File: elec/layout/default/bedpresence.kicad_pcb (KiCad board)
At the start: 2 copper layers, 40 x 40 mm, 0 parts

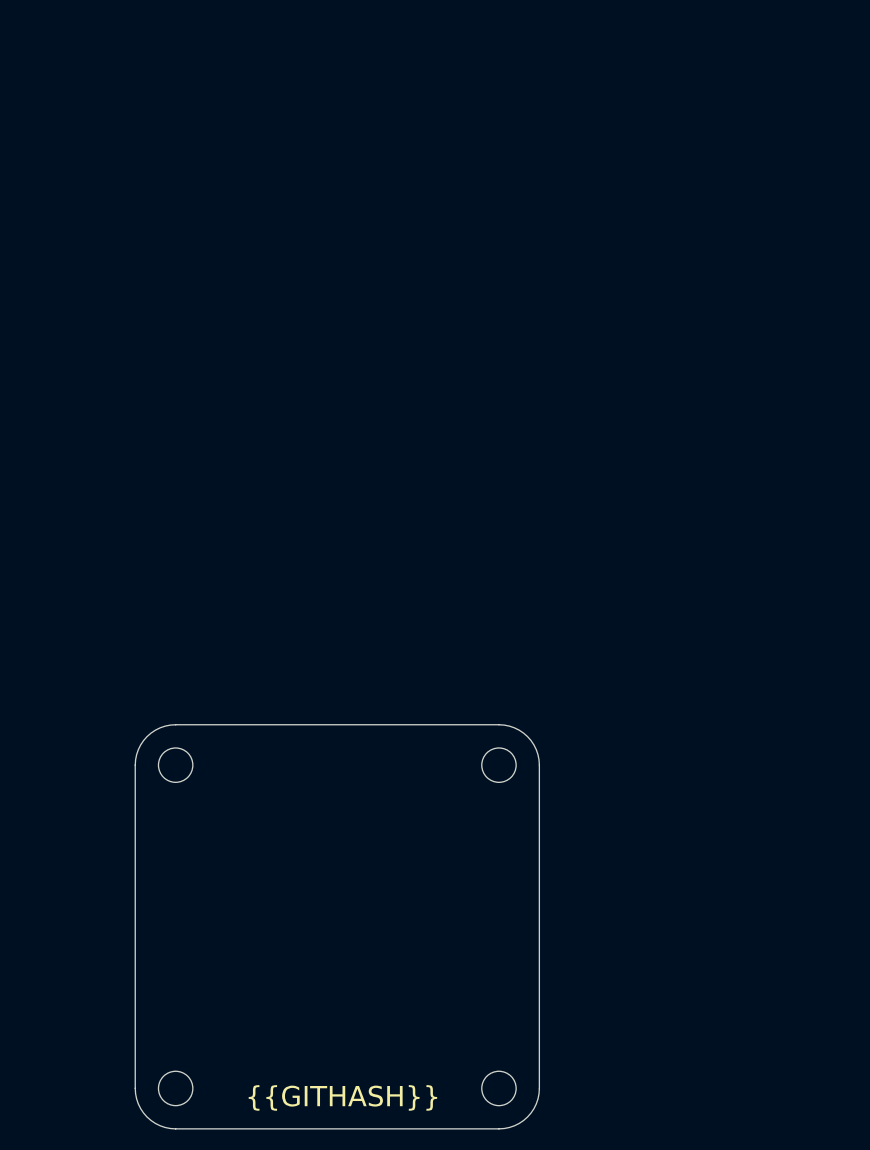
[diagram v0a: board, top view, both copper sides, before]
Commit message: Some kicad fiddling. Fix missing models. Fix their orientations etc.
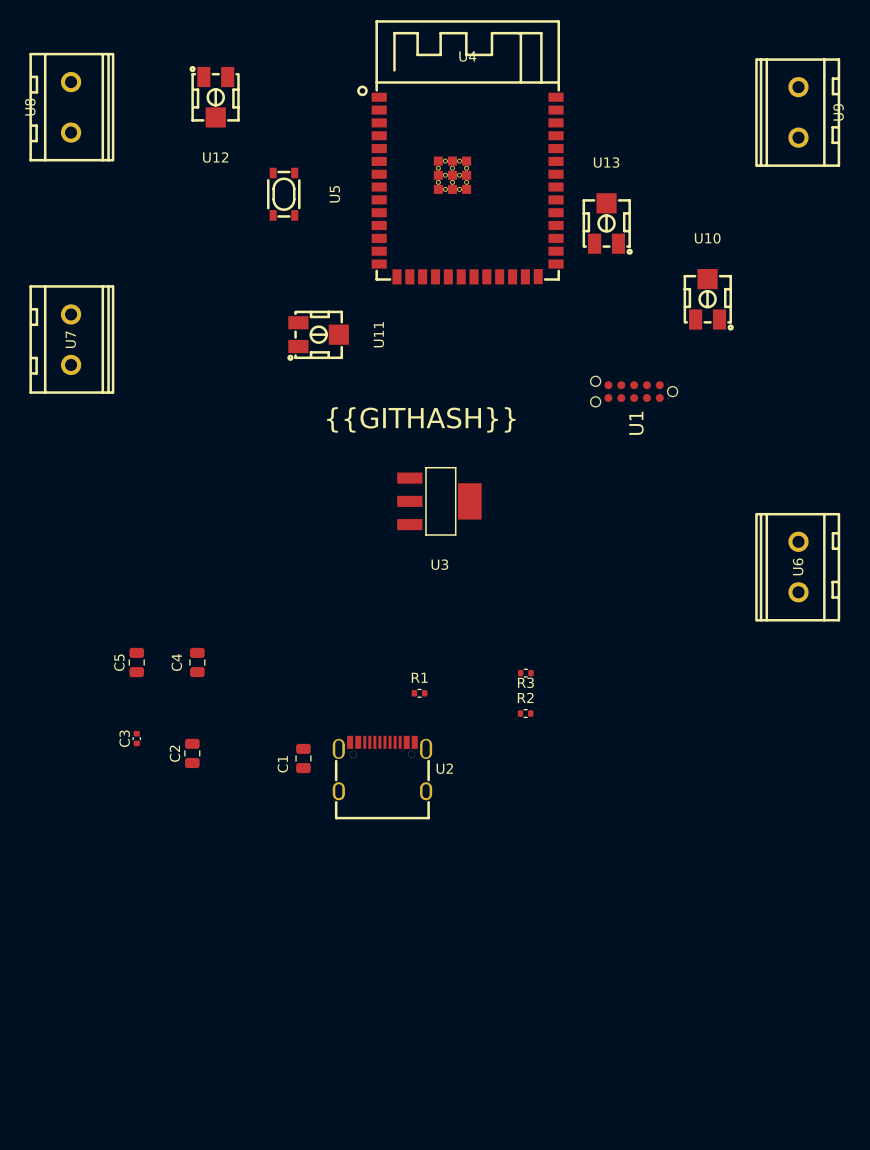
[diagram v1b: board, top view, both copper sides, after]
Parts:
- added C1: 25V 10uF X5R ±10% 0805 Multilayer Ceramic Capacitors MLCC -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, lib:C0805, F.Cu at (146.0, 81.5)
- added C2: 25V 10uF X5R ±10% 0805 Multilayer Ceramic Capacitors MLCC -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, lib:C0805, F.Cu at (135.0, 81.0)
- added C3: 16V 100nF X7R ±10% 0402 Multilayer Ceramic Capacitors MLCC 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, lib:C0402, F.Cu at (129.5, 79.5)
- added C4: 25V 10uF X5R ±10% 0805 Multilayer Ceramic Capacitors MLCC -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, lib:C0805, F.Cu at (135.5, 72.0)
- added C5: 25V 10uF X5R ±10% 0805 Multilayer Ceramic Capacitors MLCC -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, lib:C0805, F.Cu at (129.5, 72.0)
- added R1: 62.5mW Thick Film Resistors 50V ±100ppm/℃ ±1% 4.7kΩ 0402 Ch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, lib:R0402, F.Cu at (157.5, 75.0)
- added R2: 62.5mW Thick Film Resistors 50V ±100ppm/℃ ±1% 4.7kΩ 0402 Ch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, lib:R0402, F.Cu at (168.0, 77.0)
- added R3: 62.5mW Thick Film Resistors 50V ±100ppm/℃ ±1% 10kΩ 0402 Chi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, lib:R0402, F.Cu at (168.0, 73.0)
- added U1: ?, lib:TAG-CONNECT_TC2050-IDC, F.Cu at (178.7, 45.1)
- added U10: ?, lib:RES-ADJ-SMD_3314J, F.Cu at (186.0, 36.0)
- added U11: ?, lib:RES-ADJ-SMD_3314J, F.Cu at (147.5, 39.5)
- added U12: ?, lib:RES-ADJ-SMD_3314J, F.Cu at (137.3, 16.0)
- added U13: ?, lib:RES-ADJ-SMD_3314J, F.Cu at (176.0, 28.5)
- added U2: ?, lib:USB-C-SMD_KH-TYPE-C-16P, F.Cu at (153.8, 82.3)
- added U3: ?, lib:SOT-223-3_L6.5-W3.4-P2.30-LS7.0-BR, F.Cu at (159.5, 56.0)
- added U4: ?, lib:WIRELM-SMD_ESP32-S3-WROOM-1, F.Cu at (162.2, 24.9)
- added U5: ?, lib:KEY-SMD_4P-L4.2-W3.2-P2.20-LS4.6, F.Cu at (144.1, 25.6)
- added U6: ?, lib:CONN-TH_2P-P5.00_CPC3703CTR, F.Cu at (195.0, 62.5)
- added U7: ?, lib:CONN-TH_2P-P5.00_CPC3703CTR, F.Cu at (123.0, 40.0)
- added U8: ?, lib:CONN-TH_2P-P5.00_CPC3703CTR, F.Cu at (123.0, 17.0)
- added U9: ?, lib:CONN-TH_2P-P5.00_CPC3703CTR, F.Cu at (195.0, 17.5)
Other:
- board outline removed
